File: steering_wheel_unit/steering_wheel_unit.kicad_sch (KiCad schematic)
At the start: 15 parts, among them J1 MAIN_CONNECTOR, J10 MODE2_SOCKET, J11 FUEL_CELL_SOCKET, J12 JTAG_SOCKET, J13 Conn_01x09, J14 USB_C_Receptacle_USB2.0_16P, J3 HALF_GAS_SOCKET, J4 MODE1_SOCKET, J5 FULL_GAS_SOCKET, J6 SPEED_RESET_SOCKET, J7 HORN_SOCKET, J8 SC_CLOSE_SOCKET, J9 SUPPLY_SOCKET

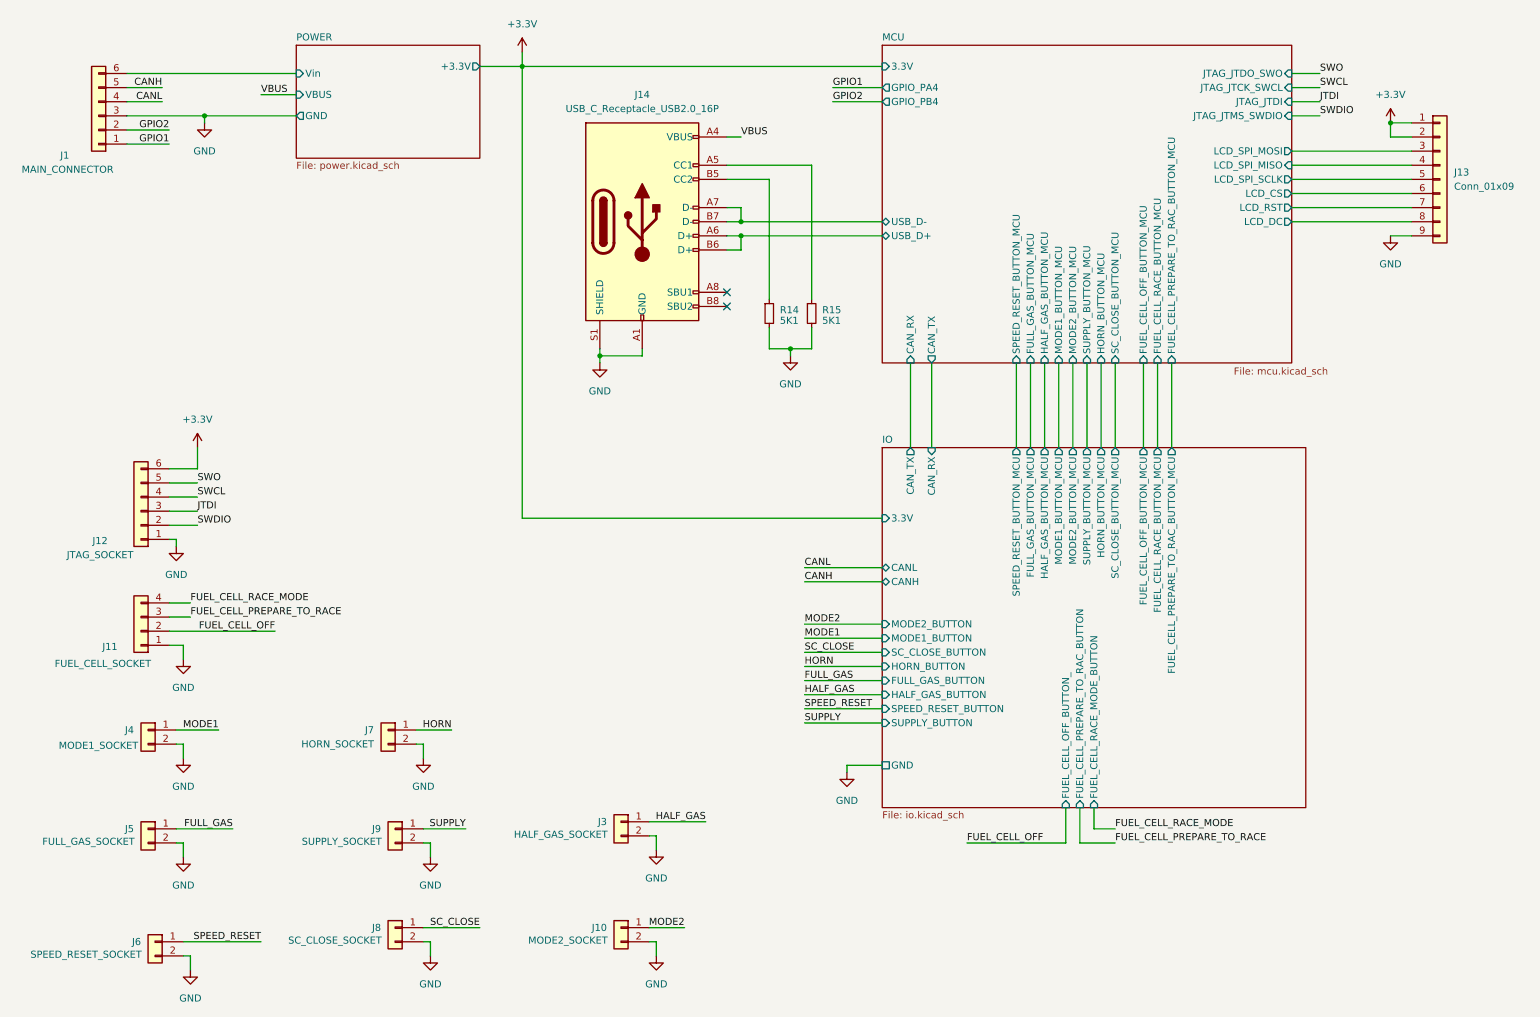
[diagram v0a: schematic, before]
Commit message: Add jtag socket and main connector, missing footprints and 3d models
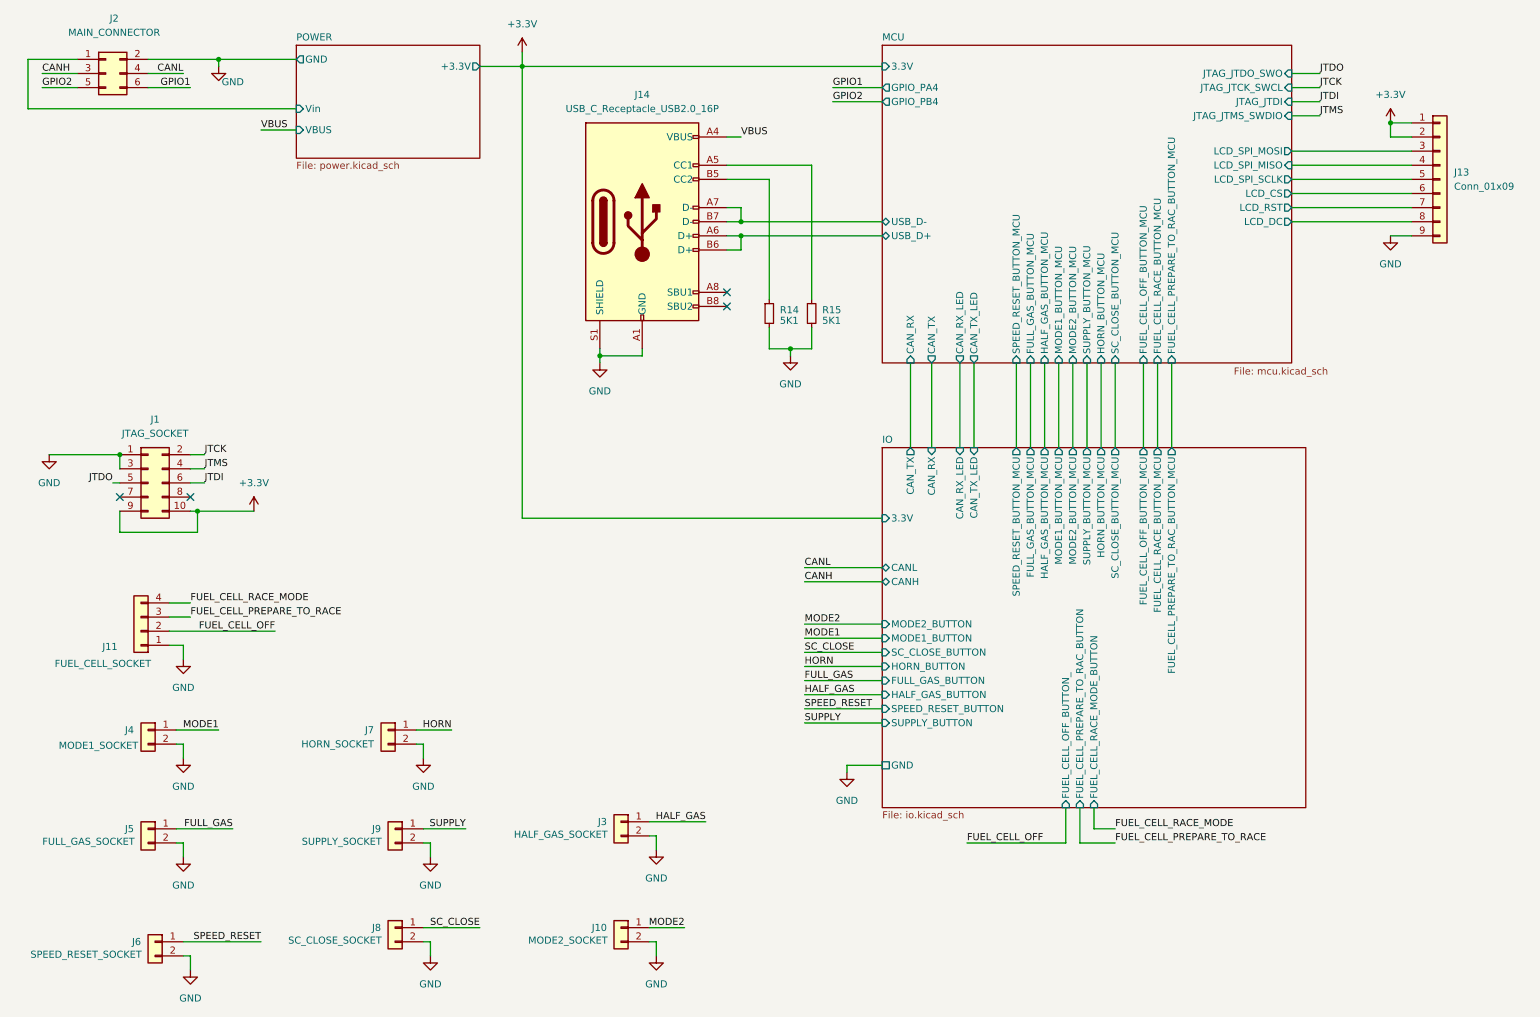
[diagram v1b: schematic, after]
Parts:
- removed J1: MAIN_CONNECTOR, symbol Connector_Generic:Conn_01x06
- removed J12: JTAG_SOCKET, symbol Connector_Generic:Conn_01x06
- added J1: JTAG_SOCKET, symbol Connector_Generic:Conn_02x05_Odd_Even
- added J2: MAIN_CONNECTOR, Lib:MOLEX_2125201006, symbol Connector_Generic:Conn_02x03_Odd_Even
- J13: footprint (none) -> Connector_JST:JST_PH_B9B-PH-K_1x09_P2.00mm_Vertical
- J14: footprint (none) -> Lib:CUI_UJ20-C-V-C-3-SMT-TR
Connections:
- net +3.3V: now also J1.10 (Pin_10), J1.9 (Pin_9)
- net CANH: now also J2.3 (Pin_3)
- net CANL: now also J2.4 (Pin_4)
- net GND: now also J1.1 (Pin_1), J1.3 (Pin_3), J2.2 (Pin_2)
- net GPIO1: now also J2.6 (Pin_6)
- net GPIO2: now also J2.5 (Pin_5)
- net JTDI: now also J1.6 (Pin_6)
- net POWER/Vin: now also J2.1 (Pin_1)
- new net JTCK: J1.2 (Pin_2)
- new net JTDO: J1.5 (Pin_5)
- new net JTMS: J1.4 (Pin_4)
- no-connect marks 2 -> 4
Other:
- sheet IO ports: added CAN_RX_LED, CAN_TX_LED; removed none
- sheet MCU ports: added CAN_RX_LED, CAN_TX_LED; removed none

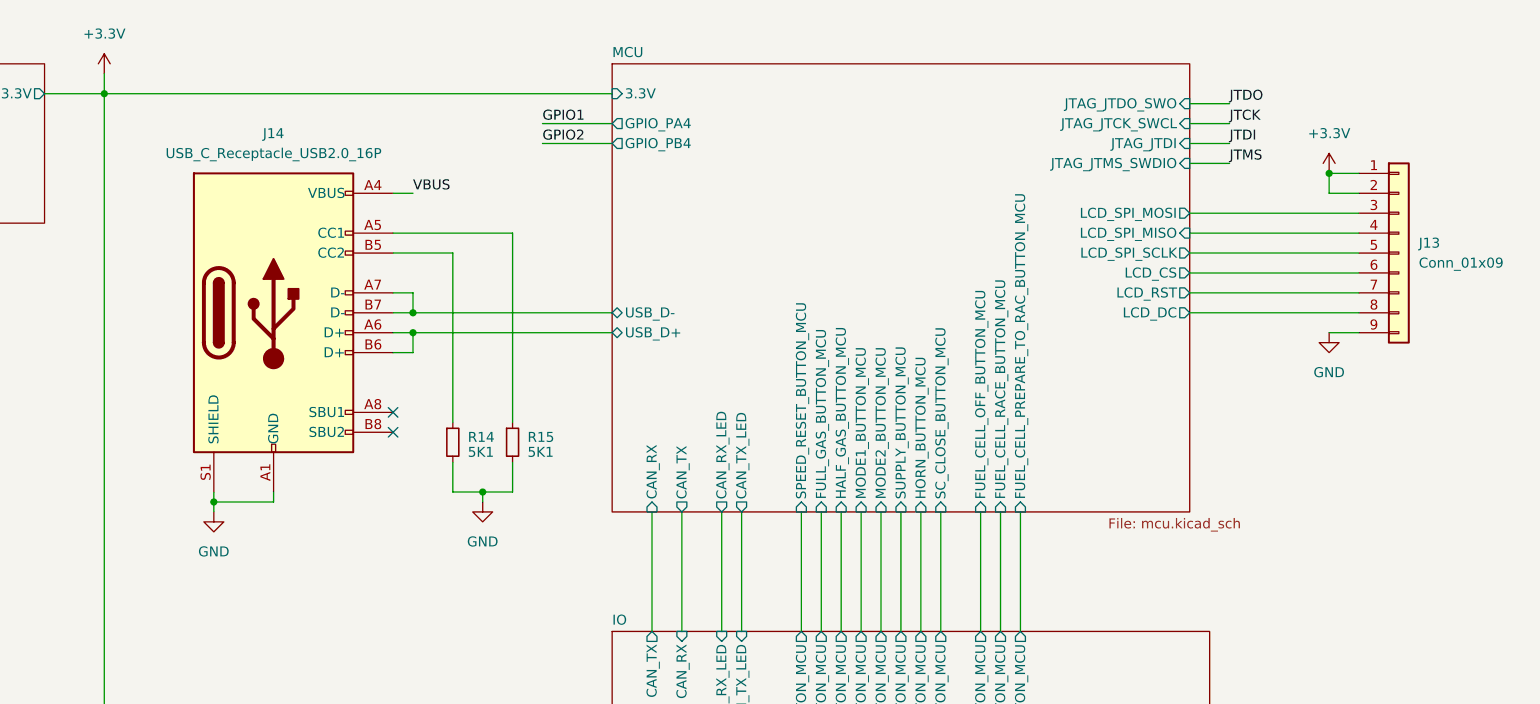
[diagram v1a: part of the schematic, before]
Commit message: change usb c connector
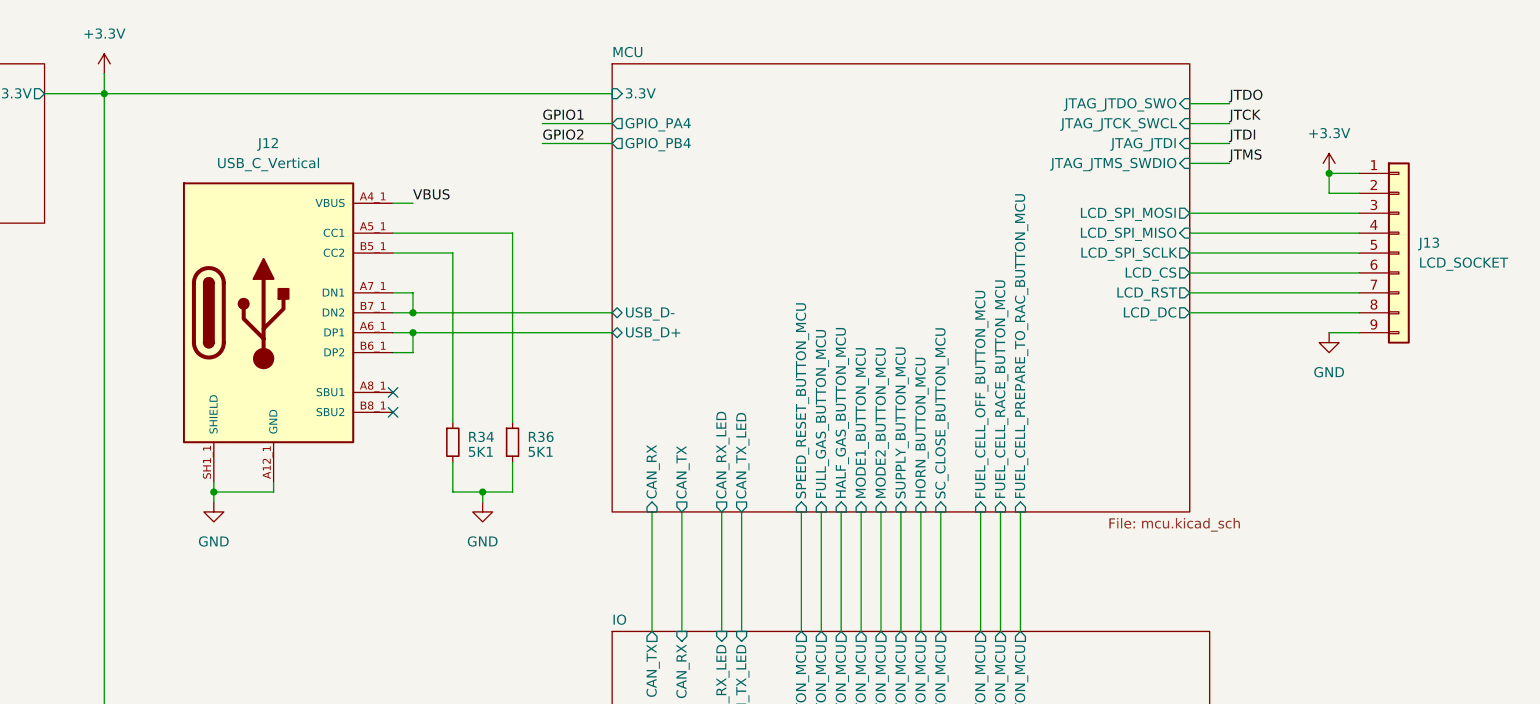
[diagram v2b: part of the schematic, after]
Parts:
- removed J14: USB_C_Receptacle_USB2.0_16P, Lib:CUI_UJ20-C-V-C-3-SMT-TR, symbol Connector:USB_C_Receptacle_USB2.0_16P
- removed R14, R15: 5K1, Resistor_SMD:R_1206_3216Metric, symbol Device:R_Small
- added J12: USB_C_Vertical, Lib:CUI_UJ20-C-V-C-3-SMT-TR, symbol UJ20-C-V-C-3-SMT-TR:UJ20-C-V-C-3-SMT-TR
- added R34, R36: 5K1, Resistor_SMD:R_1206_3216Metric, symbol Device:R_Small
- J1: footprint (none) -> Lib:61201021621
- J13: value Conn_01x09 -> LCD_SOCKET
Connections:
- net GND: now also J12.A12_1 (GND), J12.A12_2 (GND), J12.A1_1 (GND), J12.A1_2 (GND), J12.B12_1 (GND), J12.B12_2 (GND), J12.B1_1 (GND), J12.B1_2 (GND), J12.SH1_1 (SHIELD), J12.SH1_2 (SHIELD), J12.SH2_1 (SHIELD), J12.SH2_2 (SHIELD), J12.SH3_1 (SHIELD), J12.SH3_2 (SHIELD), J12.SH4_1 (SHIELD), J12.SH4_2 (SHIELD), R34.2, R36.2
- net MCU/USB_D+: now also J12.A6_1 (DP1), J12.A6_2 (DP1), J12.B6_1 (DP2), J12.B6_2 (DP2)
- net MCU/USB_D-: now also J12.A7_1 (DN1), J12.A7_2 (DN1), J12.B7_1 (DN2), J12.B7_2 (DN2)
- net VBUS: now also J12.A4_1 (VBUS), J12.A4_2 (VBUS), J12.A9_1 (VBUS), J12.A9_2 (VBUS), J12.B4_1 (VBUS), J12.B4_2 (VBUS), J12.B9_1 (VBUS), J12.B9_2 (VBUS)
- new net: J12.A5_1 (CC1), J12.A5_2 (CC1), R36.1
- new net: J12.A8_1 (SBU1), J12.A8_2 (SBU1)
- new net: J12.B5_1 (CC2), J12.B5_2 (CC2), R34.1
- new net: J12.B8_1 (SBU2), J12.B8_2 (SBU2)
